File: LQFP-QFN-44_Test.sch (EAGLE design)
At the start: 6 parts

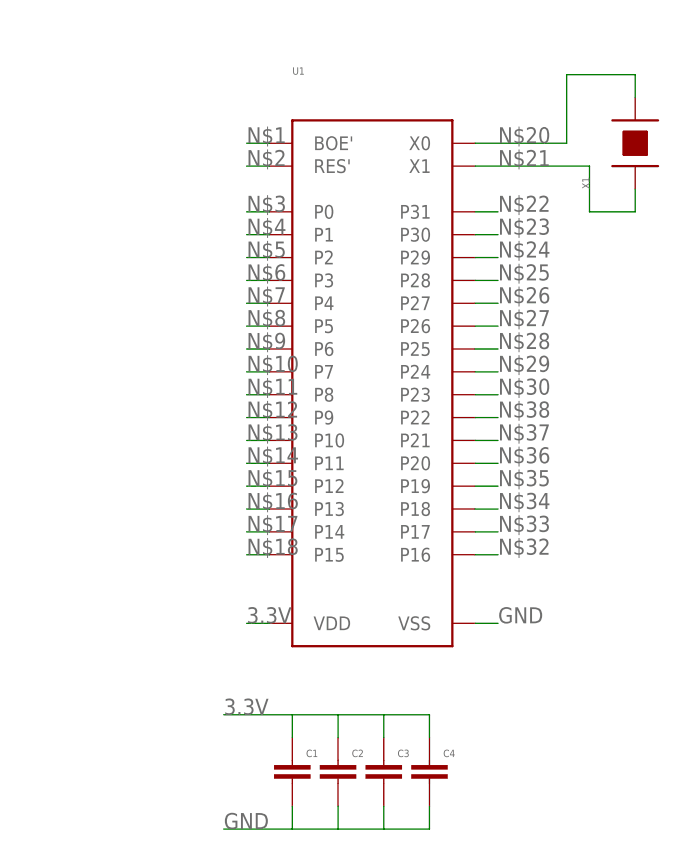
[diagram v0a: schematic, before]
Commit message: Finished the layout for the appnote.
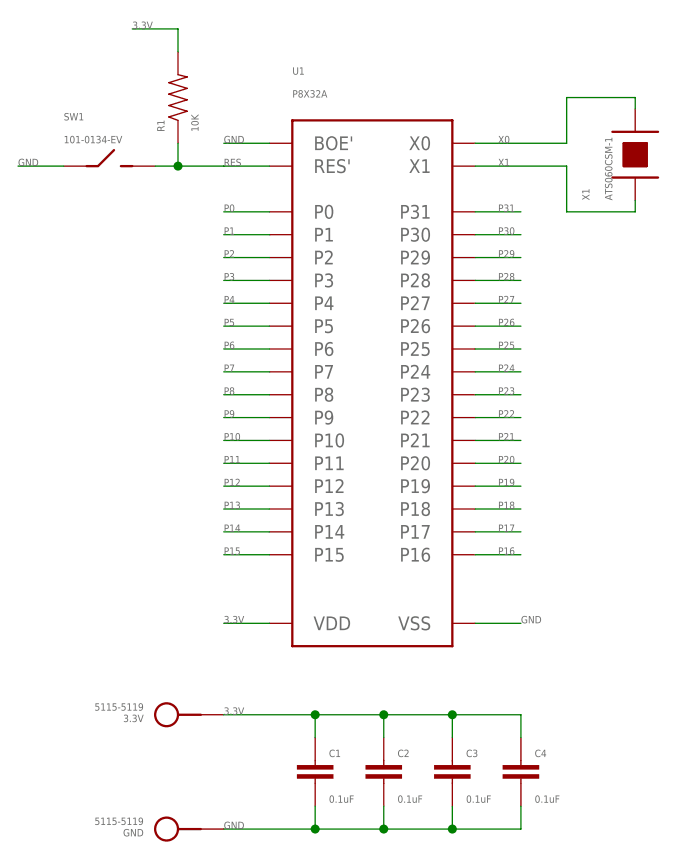
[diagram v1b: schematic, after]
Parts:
- added 3.3V, GND: 5115-5119, PP_Connectors:TEST_POINT_SINGLEKEYSTONE_5115-5119
- added R1: 10K, PP_Passives:RESISTOR0402
- added SW1: 101-0134-EV, PP_Electromechanical:SPST101-0134-EV
- C1, C2, C3, C4: value (none) -> 0.1uF
- U1: value (none) -> P8X32A
- X1: value (none) -> ATS060CSM-1; device PP_FreqCtrl:CRYSTAL7MM_X_5MM -> PP_FreqCtrl:CRYSTALHC-49
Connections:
- net N$10 renamed P7
- net N$11 renamed P8
- net N$12 renamed P9
- net N$13 renamed P10
- net N$14 renamed P11
- net N$15 renamed P12
- net N$16 renamed P13
- net N$17 renamed P14
- net N$18 renamed P15
- net N$20 renamed X0
- net N$21 renamed X1
- net N$22 renamed P31
- net N$23 renamed P30
- net N$24 renamed P29
- net N$25 renamed P28
- net N$26 renamed P27
- net N$27 renamed P26
- net N$28 renamed P25
- net N$29 renamed P24
- net N$3 renamed P0
- net N$30 renamed P23
- net N$32 renamed P16
- net N$33 renamed P17
- net N$34 renamed P18
- net N$35 renamed P19
- net N$36 renamed P20
- net N$37 renamed P21
- net N$38 renamed P22
- net N$4 renamed P1
- net N$5 renamed P2
- net N$6 renamed P3
- net N$7 renamed P4
- net N$8 renamed P5
- net N$9 renamed P6
- removed net N$1: U1.BOE'
- removed net N$2: U1.RES'
- new net RES: R1.1, SW1.B, U1.RES'
- net 3.3V: now also 3.3V.P$1, R1.2
- net GND: now also GND.P$1, SW1.A, U1.BOE'
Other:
- moved on the sheet: C1, C2, C3, C4, X1

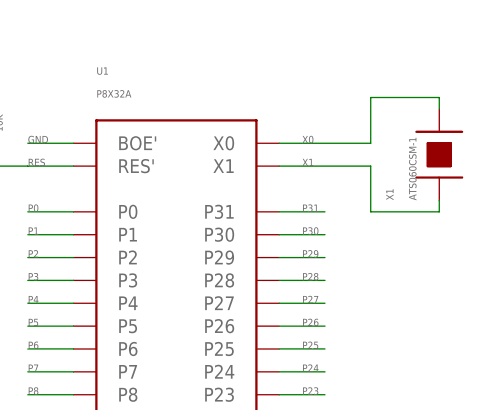
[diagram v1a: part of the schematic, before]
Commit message: Changed Crystal Value to ABLS3-6.000MHZ-D4Y-T
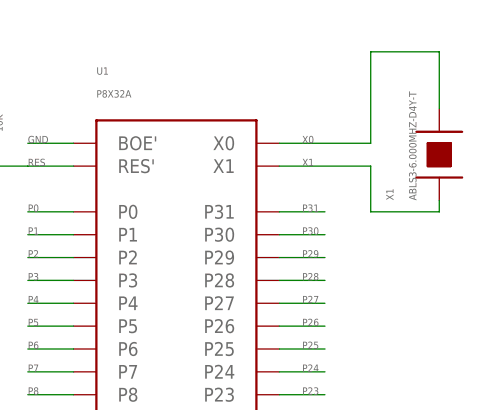
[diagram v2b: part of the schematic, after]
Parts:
- X1: value ATS060CSM-1 -> ABLS3-6.000MHZ-D4Y-T
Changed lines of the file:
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@@
 <grid distance="0.1" unitdist="inch" unit="inch" style="lines" multiple="1" display="no" altdistance="0.01" altunitdist="inch" altunit="inch"/>
 <layers>
-<layer number="1" name="Top" color="4" fill="1" visible="yes" active="no"/>
+<layer number="1" name="Top" color="4" fill="1" visible="no" active="no"/>
 <layer number="2" name="Route2" color="1" fill="3" visible="no" active="no"/>
 <layer number="3" name="Route3" color="4" fill="3" visible="no" active="no"/>
@@
 <layer number="14" name="Route14" color="1" fill="6" visible="no" active="no"/>
 <layer number="15" name="Route15" color="4" fill="6" visible="no" active="no"/>
-<layer number="16" name="Bottom" color="1" fill="1" visible="yes" active="no"/>
-<layer number="17" name="Pads" color="2" fill="1" visible="yes" active="no"/>
-<layer number="18" name="Vias" color="2" fill="1" visible="yes" active="no"/>
-<layer number="19" name="Unrouted" color="6" fill="1" visible="yes" active="no"/>
-<layer number="20" name="Dimension" color="15" fill="1" visible="yes" active="no"/>
-<layer number="21" name="tPlace" color="7" fill="1" visible="yes" active="no"/>
-<layer number="22" name="bPlace" color="7" fill="1" visible="yes" active="no"/>
-<layer number="23" name="tOrigins" color="15" fill="1" visible="yes" active="no"/>
-<layer number="24" name="bOrigins" color="15" fill="1" visible="yes" active="no"/>
-<layer number="25" name="tNames" color="7" fill="1" visible="yes" active="no"/>
-<layer number="26" name="bNames" color="7" fill="1" visible="yes" active="no"/>
-<layer number="27" name="tValues" color="7" fill="1" visible="yes" active="no"/>
-<layer number="28" name="bValues" color="7" fill="1" visible="yes" active="no"/>
+<layer number="16" name="Bottom" color="1" fill="1" visible="no" active="no"/>
+<layer number="17" name="Pads" color="2" fill="1" visible="no" active="no"/>
+<layer number="18" name="Vias" color="2" fill="1" visible="no" active="no"/>
+<layer number="19" name="Unrouted" color="6" fill="1" visible="no" active="no"/>
+<layer number="20" name="Dimension" color="15" fill="1" visible="no" active="no"/>
+<layer number="21" name="tPlace" color="7" fill="1" visible="no" active="no"/>
+<layer number="22" name="bPlace" color="7" fill="1" visible="no" active="no"/>
+<layer number="23" name="tOrigins" color="15" fill="1" visible="no" active="no"/>
+<layer number="24" name="bOrigins" color="15" fill="1" visible="no" active="no"/>
+<layer number="25" name="tNames" color="7" fill="1" visible="no" active="no"/>
+<layer number="26" name="bNames" color="7" fill="1" visible="no" active="no"/>
+<layer number="27" name="tValues" color="7" fill="1" visible="no" active="no"/>
+<layer number="28" name="bValues" color="7" fill="1" visible="no" active="no"/>
 <layer number="29" name="tStop" color="7" fill="3" visible="no" active="no"/>
 <layer number="30" name="bStop" color="7" fill="6" visible="no" active="no"/>
@@
 <layer number="35" name="tGlue" color="7" fill="4" visible="no" active="no"/>
 <layer number="36" name="bGlue" color="7" fill="5" visible="no" active="no"/>
-<layer number="37" name="tTest" color="7" fill="1" visible="yes" active="no"/>
-<layer number="38" name="bTest" color="7" fill="1" visible="yes" active="no"/>
+<layer number="37" name="tTest" color="7" fill="1" visible="no" active="no"/>
+<layer number="38" name="bTest" color="7" fill="1" visible="no" active="no"/>
 <layer number="39" name="tKeepout" color="4" fill="11" visible="no" active="no"/>
 <layer number="40" name="bKeepout" color="1" fill="11" visible="no" active="no"/>
@@
 <layer number="44" name="Drills" color="7" fill="1" visible="no" active="no"/>
 <layer number="45" name="Holes" color="7" fill="1" visible="no" active="no"/>
-<layer number="46" name="Milling" color="3" fill="1" visible="yes" active="no"/>
-<layer number="47" name="Measures" color="7" fill="1" visible="yes" active="no"/>
-<layer number="48" name="Document" color="7" fill="1" visible="yes" active="no"/>
-<layer number="49" name="Reference" color="7" fill="1" visible="yes" active="no"/>
-<layer number="50" name="dxf" color="7" fill="1" visible="yes" active="no"/>
-<layer number="51" name="tDocu" color="7" fill="1" visible="yes" active="no"/>
-<layer number="52" name="bDocu" color="7" fill="1" visible="yes" active="no"/>
-<layer number="53" name="tGND_GNDA" color="7" fill="9" visible="yes" active="no"/>
-<layer number="54" name="bGND_GNDA" color="1" fill="9" visible="yes" active="no"/>
-<layer number="56" name="wert" color="7" fill="1" visible="yes" active="no"/>
+<layer number="46" name="Milling" color="3" fill="1" visible="no" active="no"/>
+<layer number="47" name="Measures" color="7" fill="1" visible="no" active="no"/>
+<layer number="48" name="Document" color="7" fill="1" visible="no" active="no"/>
+<layer number="49" name="Reference" color="7" fill="1" visible="no" active="no"/>
+<layer number="50" name="dxf" color="7" fill="1" visible="no" active="no"/>
+<layer number="51" name="tDocu" color="7" fill="1" visible="no" active="no"/>
+<layer number="52" name="bDocu" color="7" fill="1" visible="no" active="no"/>
+<layer number="53" name="tGND_GNDA" color="7" fill="9" visible="no" active="no"/>
+<layer number="54" name="bGND_GNDA" color="1" fill="9" visible="no" active="no"/>
+<layer number="56" name="wert" color="7" fill="1" visible="no" active="no"/>
 <layer number="91" name="Nets" color="2" fill="1" visible="yes" active="yes"/>
 <layer number="92" name="Busses" color="1" fill="1" visible="yes" active="yes"/>
@@
 <part name="C3" library="PP_Passives" deviceset="CAPACITOR_NON_POLAR" device="0402" value="0.1uF"/>
 <part name="C4" library="PP_Passives" deviceset="CAPACITOR_NON_POLAR" device="0402" value="0.1uF"/>
-<part name="X1" library="PP_FreqCtrl" deviceset="CRYSTAL" device="HC-49" value="ATS060CSM-1"/>
+<part name="X1" library="PP_FreqCtrl" deviceset="CRYSTAL" device="HC-49" value="ABLS3-6.000MHZ-D4Y-T"/>
 <part name="R1" library="PP_Passives" deviceset="RESISTOR" device="0402" value="10K"/>
 <part name="SW1" library="PP_Electromechanical" deviceset="SPST" device="101-0134-EV" value="101-0134-EV"/>
@@
 <label x="27.94" y="58.42" size="0.8128" layer="95" font="vector"/>
 <wire x1="25.4" y1="58.42" x2="35.56" y2="58.42" width="0.1524" layer="91"/>
-<wire x1="35.56" y1="58.42" x2="35.56" y2="63.5" width="0.1524" layer="91"/>
+<wire x1="35.56" y1="58.42" x2="35.56" y2="68.58" width="0.1524" layer="91"/>
 <pinref part="X1" gate="G$1" pin="P$2"/>
-<wire x1="35.56" y1="63.5" x2="43.18" y2="63.5" width="0.1524" layer="91"/>
-<wire x1="43.18" y1="63.5" x2="43.18" y2="62.23" width="0.1524" layer="91"/>
-</segment>
-</net>
+<wire x1="35.56" y1="68.58" x2="43.18" y2="68.58" width="0.1524" layer="91"/>
+<wire x1="43.18" y1="68.58" x2="43.18" y2="62.23" width="0.1524" layer="91"/>
+</segment>
+</net>
